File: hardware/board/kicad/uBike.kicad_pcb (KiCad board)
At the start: 2 copper layers, 60 x 80 mm, 60 parts, among them J1 KMDGX-6S-BS, J2 F31S-1A7L1-11040, J3 KMDGX-8S-BS, J4 TC2050-IDC-NL, J5 87520-0010BLF, Q1 MMBT3904, U1 SN65HVD08DR, U2 LD1117S33TR_SOT223, U3 MDBT50Q-P1MV2, U4 PTPSM863252RDXR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

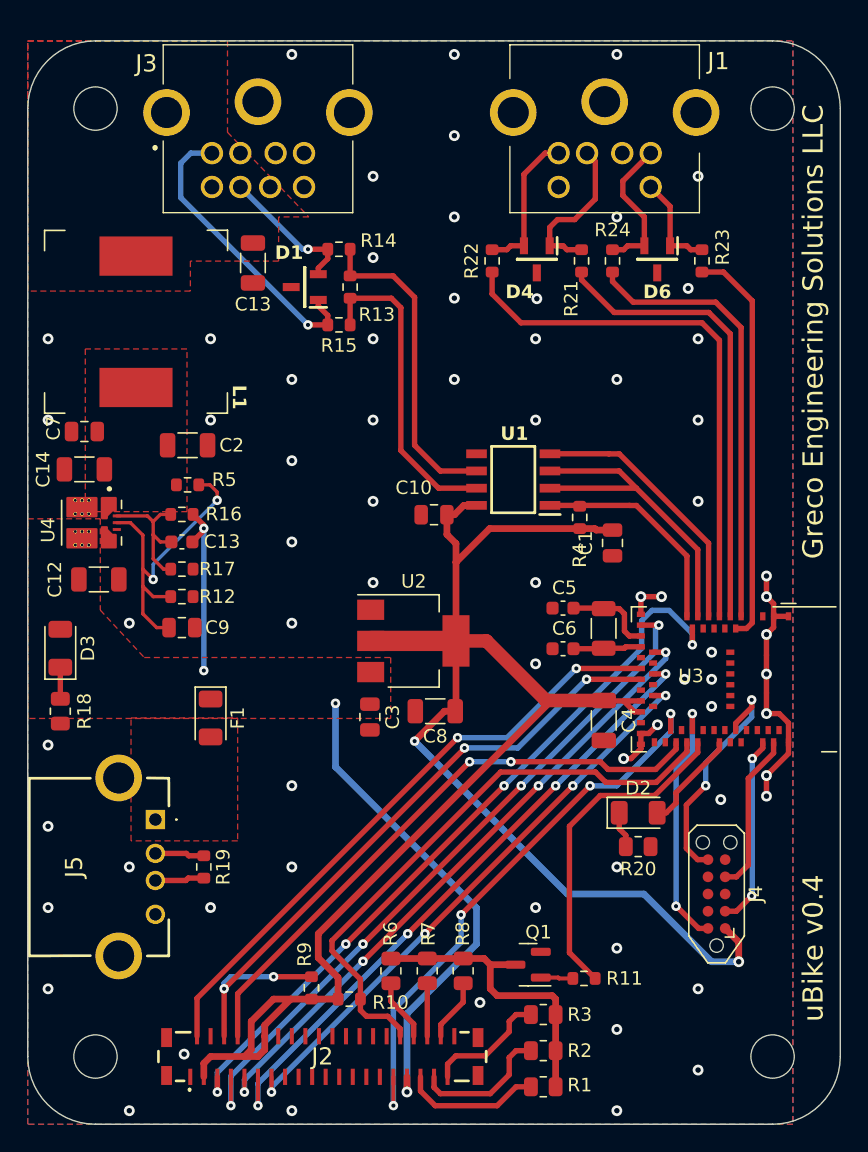
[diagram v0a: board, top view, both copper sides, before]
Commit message: First pass at LM2596 regulator
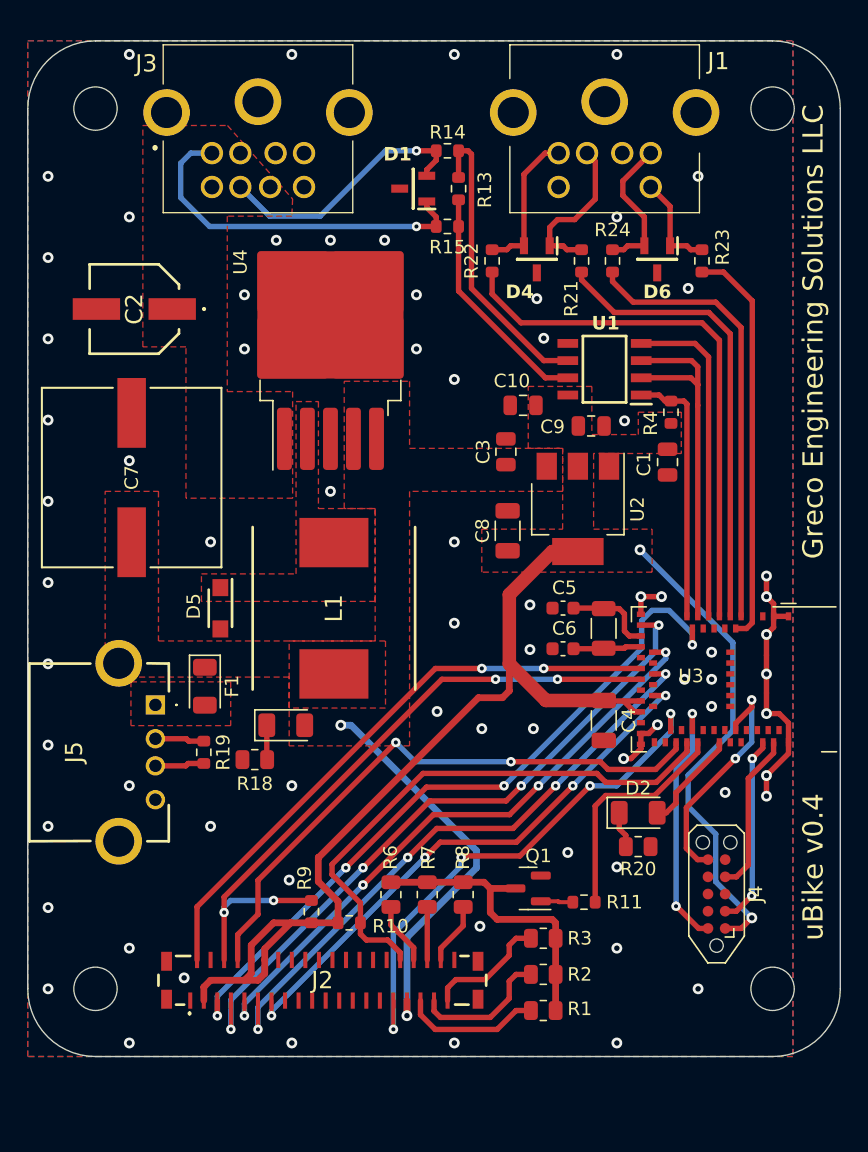
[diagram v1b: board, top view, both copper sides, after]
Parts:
- removed C11: 22p, Capacitor_SMD:C_0603_1608Metric
- removed C12: 33u, Capacitor_SMD:C_1206_3216Metric
- removed C13, C14: 2u2, Capacitor_SMD:C_1206_3216Metric
- removed R12: 10k, Resistor_SMD:R_0603_1608Metric
- removed R16: 220k, Resistor_SMD:R_0603_1608Metric
- removed R17: 30k, Resistor_SMD:R_0603_1608Metric
- removed R5: 61.9k, Resistor_SMD:R_0603_1608Metric
- added D5: SS24FL, libs:SODFL3617X108N, F.Cu at (69.2, 66.9)
- C10: value 100n -> 1u
- C2: value 10u -> 120u; footprint Capacitor_SMD:C_1206_3216Metric -> libs:16SVF180M
- C7: value 100n -> 220u; footprint Capacitor_SMD:C_0805_2012Metric -> libs:CHEMI-KE0
- C9: value 10n -> 100n
- L1: value 120u -> MSS1210-683MED; footprint libs:L_Bourns_5050 -> libs:INDPM120120X1020N
- R13: value 120 -> 250
- R18: value 150 -> 330
- U4: value PTPSM863252RDXR -> LM2596S-5; footprint libs:TPSM863252RDX -> Package_TO_SOT_SMD:TO-263-5_TabPin3
- moved C9 33.7 mm to (96.6, 53.4), turned to 180 degrees
- moved L1 25.7 mm to (77.6, 66.9)
- moved U4 22.5 mm to (77.4, 46.7), turned to 90 degrees
- moved C3 22.0 mm to (90.3, 55.3), turned to 90 degrees
- moved D3 17.6 mm to (74.0, 75.5), turned to 0 degrees
- moved U2 15.6 mm to (95.6, 59.6), turned to -90 degrees
- moved R18 14.8 mm to (71.8, 78.1), turned to 0 degrees
- moved C8 14.4 mm to (90.4, 61.2), turned to 90 degrees
- moved D1 10.8 mm to (83.5, 35.9)
- moved R13 10.8 mm to (86.8, 35.9)
- moved R14 10.8 mm to (86.0, 33.1)
- moved R15 10.8 mm to (86.0, 38.7)
- moved C2 10.8 mm to (62.9, 44.8), turned to 90 degrees
- moved U1 10.6 mm to (97.6, 49.2)
- moved C10 10.4 mm to (91.6, 51.9)
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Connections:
- C7 pad 1: +12V -> +5V
- C9 pad 1: Net-(U4-EN) -> GND
- C9 pad 2: GND -> +3.3V
- J3 pad 1: 12_VIN -> +12V
- J3 pad 7: 12_VIN -> +12V
- L1 pad 1: 12_VIN -> Net-(D5-K)
- L1 pad 2: +12V -> +5V
- U4 pad 2: unconnected-(U4-SW-Pad2) -> Net-(D5-K)
- U4 pad 3: +5V -> GND
- U4 pad 4: GND -> +5V
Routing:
- net +3.3V: track 144.7 -> 110.4 mm
- net Net-(U4-EN): track 23.9 -> 0.00 mm, vias 2 -> 0
- net +5V: track 49.5 -> 29.3 mm, vias 4 -> 2
- net Net-(U4-FB): track 10.3 -> 0.00 mm
- net RS485_A: track 10.5 -> 19.5 mm
- net BL_PWM: track 24.5 -> 17.1 mm
- net Net-(U1-B): track 23.3 -> 17.5 mm
- net RS485_B: track 22.0 -> 27.0 mm
- net TX: track 19.8 -> 24.5 mm
- net RX: track 16.1 -> 19.3 mm
- net YU: track 41.9 -> 38.8 mm
- net DE: track 24.6 -> 27.2 mm
- net CTP_SDA: track 43.4 -> 41.0 mm
- net SDO: track 43.5 -> 41.2 mm
- net RESET: track 52.0 -> 49.7 mm
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- added copper zone on F.Cu, net +3.3V
- added copper zone on F.Cu, net Net-(D5-K)
- removed copper zone on F.Cu, net 12_VIN
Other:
- board size 60 x 80 mm -> 60 x 75 mm
- board text removed: "C13"

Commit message: Some general cleanup
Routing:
- net SWO: track 17.6 -> 24.4 mm
- net GND: track 26.7 -> 20.8 mm, vias 71 -> 81
- net +3.3V: track 110.4 -> 109.5 mm
